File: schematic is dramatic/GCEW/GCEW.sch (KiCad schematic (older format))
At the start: 50 parts, among them J1 Conn_01x09_Male, J2 Conn_02x03_Odd_Even, J3 Conn_02x03_Odd_Even, J4 Conn_02x02_Odd_Even, M1 BLDC_Motor, U1 LM26CIM5-VHA, U2 DRV8323RH, U3 IPB029N06N, U4 IPB029N06N, U5 IPB029N06N, U6 IPB029N06N, U7 IPB029N06N, U8 IPB029N06N, U9 BLDC_Hall_Sensor

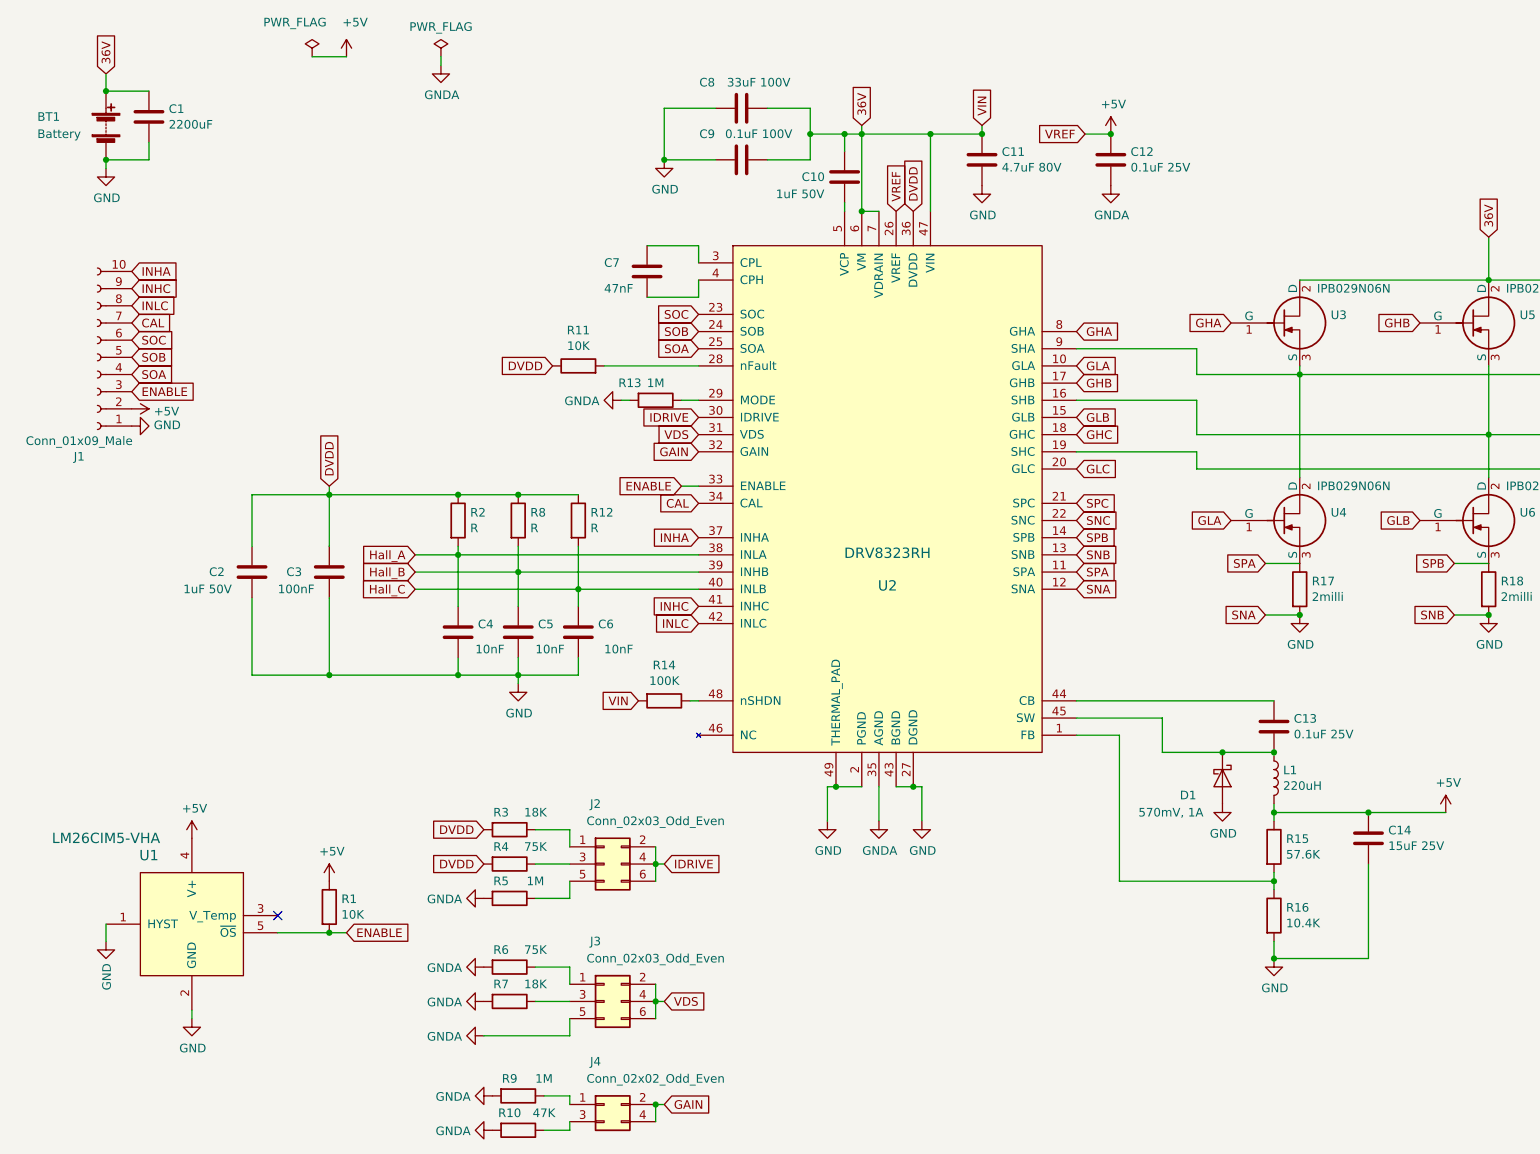
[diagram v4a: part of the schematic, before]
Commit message: GCEW Motor Controller Schematic Update 5
Finalized KiCAD GCEW Motor Controller Schematic. Initial KiCAD Motor Controller PCB Design.
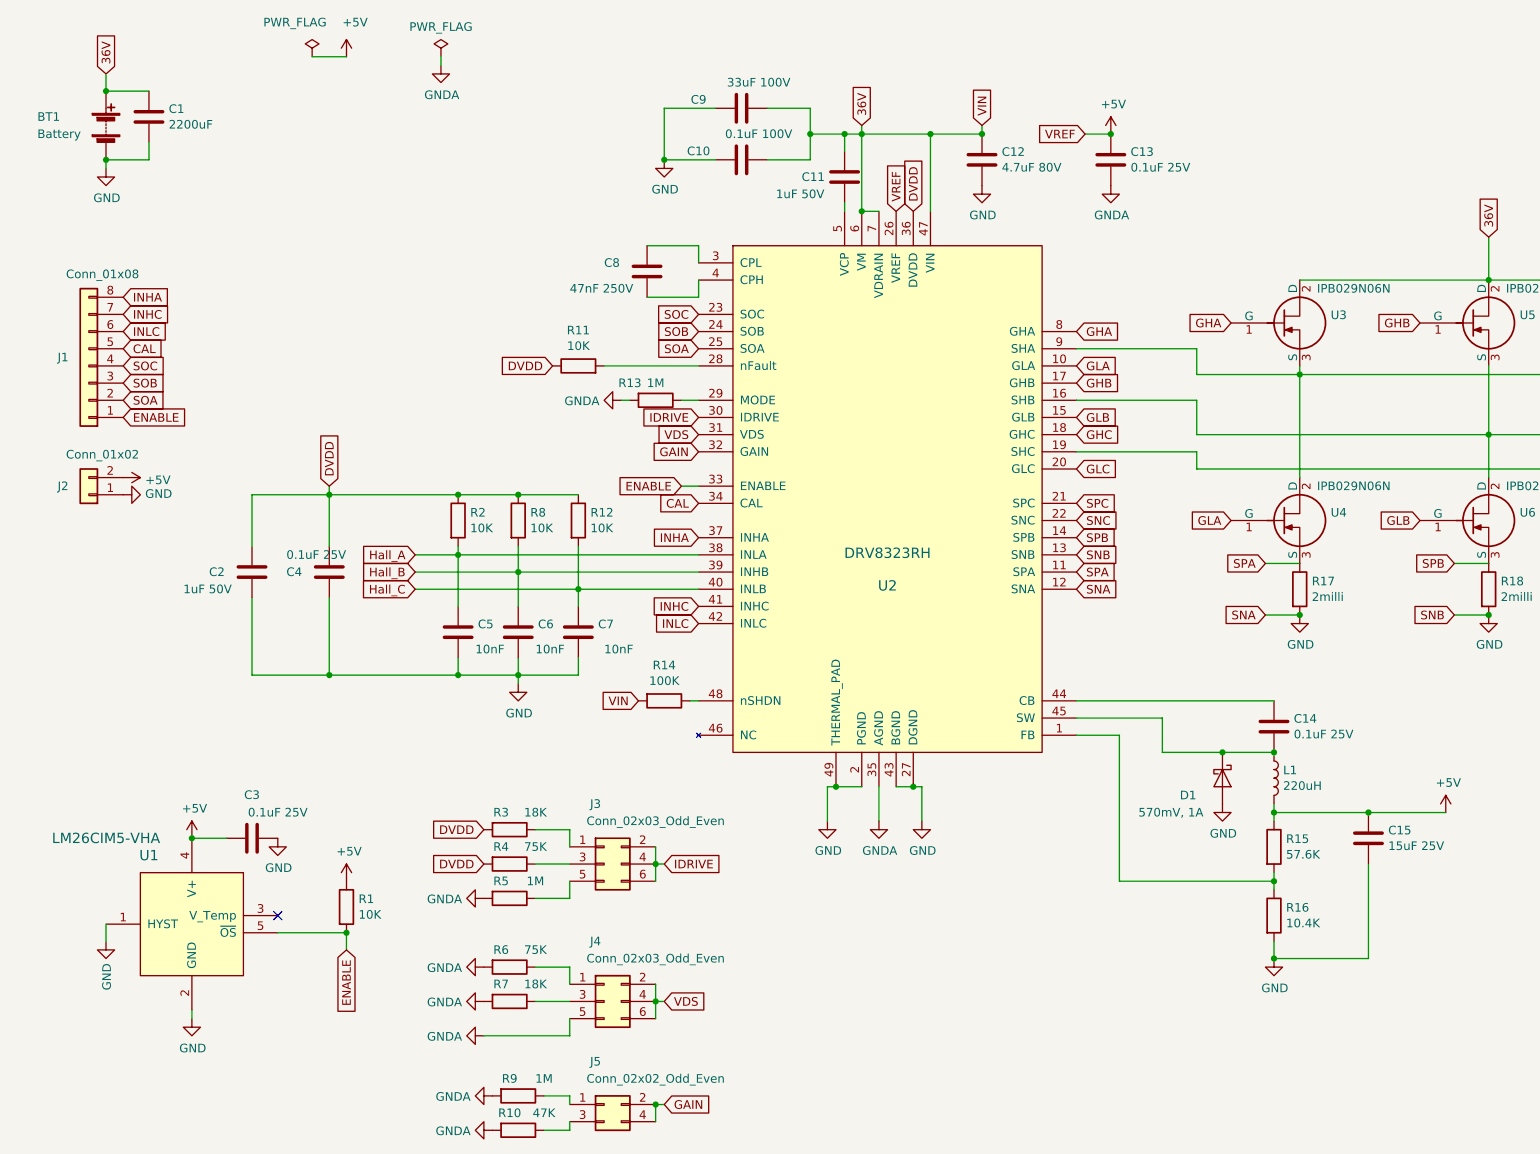
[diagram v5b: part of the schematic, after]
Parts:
- removed J1: Conn_01x09_Male, symbol Connector:Conn_01x10_Female
- added C3: 0.1uF 25V, Capacitors_SMD:C_1206, symbol Device:C
- added J1: Conn_01x08, myLib:PhoenixContact_1985027_8-Pin-Connector_8A_P3.5mm, symbol Connector_Generic:Conn_01x08
- added J2: Conn_01x02, myLib:PhoenixContact_1984963_2-Pin-Connector_8A_P3.5mm, symbol Connector_Generic:Conn_01x02
- BT1: footprint (none) -> myLib:PhoenixContact_1935776_2-Pin-Connector_32A_P5mm
- C1: footprint Capacitor_THT:CP_Radial_D18.0mm_P7.50mm -> Capacitors_THT:CP_Radial_D18.0mm_P7.50mm
- C10: renamed from C9; footprint Capacitor_SMD:C_1206_3216Metric -> Capacitors_SMD:C_1206
- C11: renamed from C10; footprint Capacitor_SMD:C_1206_3216Metric -> Capacitors_SMD:C_1206
- C12: renamed from C11; footprint CAPAE430X550N:CAPAE430X550N -> myLib:CP_Elec_6.6x6.6mm
- C13: renamed from C12; footprint Capacitor_SMD:C_1206_3216Metric -> Capacitors_SMD:C_1206
- C14: renamed from C13; footprint Capacitor_SMD:C_1206_3216Metric -> Capacitors_SMD:C_1206
- C15: renamed from C14; footprint 25TQC15MYFB:CAPPM3528X200N -> myLib:CP_Tantalum_Case-3528
- C2: footprint Capacitor_SMD:C_1206_3216Metric -> Capacitors_SMD:C_1206
- C4: renamed from C3; value 100nF -> 0.1uF 25V; footprint Capacitor_SMD:C_1206_3216Metric -> Capacitors_SMD:C_1206
- C5: renamed from C4; footprint Capacitor_SMD:C_1206_3216Metric -> Capacitors_SMD:C_0805
- C6: renamed from C5; footprint Capacitor_SMD:C_1206_3216Metric -> Capacitors_SMD:C_0805
- C7: renamed from C6; footprint Capacitor_SMD:C_1206_3216Metric -> Capacitors_SMD:C_0805
- C8: renamed from C7; value 47nF -> 47nF 250V; footprint Capacitor_SMD:C_1206_3216Metric -> Capacitors_SMD:C_1206
- C9: renamed from C8; footprint Capacitor_THT:CP_Radial_D10.0mm_P5.00mm -> Capacitors_THT:CP_Radial_D10.0mm_P5.00mm
- D1: footprint SOT1061:SOT1061 -> Diodes_SMD:D_SOD-123F
- J3: renamed from J2; footprint (none) -> Pin_Headers:Pin_Header_Straight_2x03_Pitch2.54mm
- J4: renamed from J3; footprint (none) -> Pin_Headers:Pin_Header_Straight_2x03_Pitch2.54mm
- J5: renamed from J4; footprint (none) -> Pin_Headers:Pin_Header_Straight_2x02_Pitch2.54mm
- L1: footprint CLF10060NIT-1R0N-D:INDPM101100X630N -> myLib:CLF10060NIT-221M-D
- M1: footprint (none) -> myLib:PhoenixContact_1991309_3-Pin-Connector_32A_P5mm
- R1, R10, R11, R13, R14, R3, R4, R5, R6, R7, R9: footprint Resistor_SMD:R_1206_3216Metric -> Resistors_SMD:R_1206
- R12, R2, R8: value R -> 10K; footprint Resistor_SMD:R_1206_3216Metric -> Resistors_SMD:R_1206
- R15, R16: footprint Resistor_SMD:R_0805_2012Metric -> Resistors_SMD:R_0805
- R17, R18, R19: footprint Resistor_SMD:R_1206_3216Metric -> Resistors_SMD:R_2512
- U1: footprint Package_TO_SOT_SMD:SOT-23-5 -> myLib:SOT-23-5
- U3, U4, U5, U6, U7, U8: footprint Package_TO_SOT_SMD:TO-263-2 -> myLib:TO-263-2
- U9: footprint (none) -> myLib:PhoenixContact_1984992_5-Pin-Connector_8A_P3.5mm
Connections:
- net +5V: now also C3.2, J2.2 (Pin_2)
- net CAL: now also J1.5 (Pin_5)
- net ENABLE: now also J1.1 (Pin_1)
- net GND: now also C3.1, J2.1 (Pin_1)
- net INHA: now also J1.8 (Pin_8)
- net INHC: now also J1.7 (Pin_7)
- net INLC: now also J1.6 (Pin_6)
- net SOA: now also J1.2 (Pin_2)
- net SOB: now also J1.3 (Pin_3)
- net SOC: now also J1.4 (Pin_4)
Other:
- moved on the sheet: R1

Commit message: GCEW Motor Controller Schematic Update 5
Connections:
- net GNDA is gone; now on net GND: C13.2, J4.5 (Pin_5), R10.2, R13.2, R5.2, R6.2, R7.2, R9.2, U2.35 (AGND)
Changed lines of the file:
@@
 	4450 1900 4150 1900
 $Comp
-L power:GNDA #PWR021
+L power:GNDA #PWR022
 U 1 1 5BDA2FAD
 P 5500 5250
-F 0 "#PWR021" H 5500 5000 50  0001 C CNN
+F 0 "#PWR022" H 5500 5000 50  0001 C CNN
 F 1 "GNDA" H 5505 5077 50  0000 C CNN
 F 2 "" H 5500 5250 50  0001 C CNN
@@
 	5500 5250 5500 5050
 $Comp
-L power:GND #PWR022
+L power:GND #PWR023
 U 1 1 5BDA32CC
 P 5750 5250
-F 0 "#PWR022" H 5750 5000 50  0001 C CNN
+F 0 "#PWR023" H 5750 5000 50  0001 C CNN
 F 1 "GND" H 5755 5077 50  0000 C CNN
 F 2 "" H 5750 5250 50  0001 C CNN
@@
 $EndComp
 $Comp
-L power:GND #PWR020
+L power:GND #PWR021
 U 1 1 5BDA3307
 P 5200 5250
-F 0 "#PWR020" H 5200 5000 50  0001 C CNN
+F 0 "#PWR021" H 5200 5000 50  0001 C CNN
 F 1 "GND" H 5205 5077 50  0000 C CNN
 F 2 "" H 5200 5250 50  0001 C CNN
@@
 $EndComp
 $Comp
-L power:+5V #PWR029
+L power:+5V #PWR030
 U 1 1 5BDA56B5
 P 8800 5200
-F 0 "#PWR029" H 8800 5050 50  0001 C CNN
+F 0 "#PWR030" H 8800 5050 50  0001 C CNN
 F 1 "+5V" H 8815 5373 50  0000 C CNN
 F 2 "" H 8800 5200 50  0001 C CNN
@@
 	6900 4750 6650 4750
 $Comp
-L power:GND #PWR027
+L power:GND #PWR028
 U 1 1 5BDA6FAD
 P 7800 6050
-F 0 "#PWR027" H 7800 5800 50  0001 C CNN
+F 0 "#PWR028" H 7800 5800 50  0001 C CNN
 F 1 "GND" H 7805 5877 50  0000 C CNN
 F 2 "" H 7800 6050 50  0001 C CNN
@@
 Hall_C
 $Comp
-L power:GND #PWR033
+L power:GND #PWR034
 U 1 1 5BDAD196
 P 12550 3200
-F 0 "#PWR033" H 12550 2950 50  0001 C CNN
+F 0 "#PWR034" H 12550 2950 50  0001 C CNN
 F 1 "GND" H 12555 3027 50  0000 C CNN
 F 2 "" H 12550 3200 50  0001 C CNN
@@
 $EndComp
 $Comp
-L power:+5V #PWR032
+L power:+5V #PWR033
 U 1 1 5BDAD1EB
 P 12550 2800
-F 0 "#PWR032" H 12550 2650 50  0001 C CNN
+F 0 "#PWR033" H 12550 2650 50  0001 C CNN
 F 1 "+5V" H 12565 2973 50  0000 C CNN
 F 2 "" H 12550 2800 50  0001 C CNN
@@
 Text GLabel 6650 3700 2    50   Input ~ 0
 SNB
-Text GLabel 6650 3900 2    50   Input ~ 0
-SNA
 $Comp
 L Device:R R17
@@
 $EndComp
 $Comp
-L power:GND #PWR028
+L power:GND #PWR029
 U 1 1 5BDC102D
 P 7950 4050
-F 0 "#PWR028" H 7950 3800 50  0001 C CNN
+F 0 "#PWR029" H 7950 3800 50  0001 C CNN
 F 1 "GND" H 7955 3877 50  0000 C CNN
 F 2 "" H 7950 4050 50  0001 C CNN
@@
 	7950 4050 7750 4050
 Connection ~ 7950 4050
-Text GLabel 7750 4050 0    50   Input ~ 0
-SNA
 $Comp
 L Device:R R18
@@
 $EndComp
 $Comp
-L power:GND #PWR030
+L power:GND #PWR031
 U 1 1 5BDC23F0
 P 9050 4050
-F 0 "#PWR030" H 9050 3800 50  0001 C CNN
+F 0 "#PWR031" H 9050 3800 50  0001 C CNN
 F 1 "GND" H 9055 3877 50  0000 C CNN
 F 2 "" H 9050 4050 50  0001 C CNN
@@
 $EndComp
 $Comp
-L power:GND #PWR031
+L power:GND #PWR032
 U 1 1 5BDC242B
 P 10150 4050
-F 0 "#PWR031" H 10150 3800 50  0001 C CNN
+F 0 "#PWR032" H 10150 3800 50  0001 C CNN
 F 1 "GND" H 10155 3877 50  0000 C CNN
 F 2 "" H 10150 4050 50  0001 C CNN
@@
 	3750 3900 3750 3650
 $Comp
-L power:GND #PWR017
+L power:GND #PWR018
 U 1 1 5BE040E2
 P 3400 4450
-F 0 "#PWR017" H 3400 4200 50  0001 C CNN
+F 0 "#PWR018" H 3400 4200 50  0001 C CNN
 F 1 "GND" H 3405 4277 50  0000 C CNN
 F 2 "" H 3400 4450 50  0001 C CNN
@@
 Wire Wire Line
 	2400 800  2200 800
-$Comp
-L power:PWR_FLAG #FLG02
-U 1 1 5BE266D4
-P 2950 800
-F 0 "#FLG02" H 2950 875 50  0001 C CNN
-F 1 "PWR_FLAG" H 2950 974 50  0000 C CNN
-F 2 "" H 2950 800 50  0001 C CNN
-F 3 "~" H 2950 800 50  0001 C CNN
-	1    2950 800
-	1    0    0    -1
-$EndComp
-$Comp
-L power:GNDA #PWR010
-U 1 1 5BE2678E
-P 2950 850
-F 0 "#PWR010" H 2950 600 50  0001 C CNN
-F 1 "GNDA" H 2955 677 50  0000 C CNN
-F 2 "" H 2950 850 50  0001 C CNN
-F 3 "" H 2950 850 50  0001 C CNN
-	1    2950 850
-	1    0    0    -1
-$EndComp
-Wire Wire Line
-	2950 850  2950 800
 Text GLabel 2800 3700 0    50   Input ~ 0
 Hall_A
@@
 $EndComp
 $Comp
-L power:GND #PWR023
+L power:GND #PWR024
 U 1 1 5BD121CF
 P 6100 1550
-F 0 "#PWR023" H 6100 1300 50  0001 C CNN
+F 0 "#PWR024" H 6100 1300 50  0001 C CNN
 F 1 "GND" H 6105 1377 50  0000 C CNN
 F 2 "" H 6100 1550 50  0001 C CNN
@@
 	4350 2800 4450 2800
 $Comp
-L power:GNDA #PWR018
+L power:GNDA #PWR019
 U 1 1 5BD271E0
 P 4000 2800
-F 0 "#PWR018" H 4000 2550 50  0001 C CNN
+F 0 "#PWR019" H 4000 2550 50  0001 C CNN
 F 1 "GNDA" V 4005 2673 50  0000 R CNN
 F 2 "" H 4000 2800 50  0001 C CNN
@@
 	3700 7050 3700 7000
 $Comp
-L power:GNDA #PWR016
+L power:GNDA #PWR017
 U 1 1 5BD62495
 P 3250 7050
-F 0 "#PWR016" H 3250 6800 50  0001 C CNN
+F 0 "#PWR017" H 3250 6800 50  0001 C CNN
 F 1 "GNDA" V 3255 6923 50  0000 R CNN
 F 2 "" H 3250 7050 50  0001 C CNN
@@
 $EndComp
 $Comp
-L power:GNDA #PWR015
+L power:GNDA #PWR016
 U 1 1 5BD62647
 P 3250 6850
-F 0 "#PWR015" H 3250 6600 50  0001 C CNN
+F 0 "#PWR016" H 3250 6600 50  0001 C CNN
 F 1 "GNDA" V 3255 6723 50  0000 R CNN
 F 2 "" H 3250 6850 50  0001 C CNN
@@
 DVDD
 $Comp
-L power:GNDA #PWR011
+L power:GNDA #PWR012
 U 1 1 5BD6A69F
 P 3200 5700
-F 0 "#PWR011" H 3200 5450 50  0001 C CNN
+F 0 "#PWR012" H 3200 5450 50  0001 C CNN
 F 1 "GNDA" V 3205 5573 50  0000 R CNN
 F 2 "" H 3200 5700 50  0001 C CNN
@@
 	3700 5700 3700 5600
 $Comp
-L power:GNDA #PWR014
+L power:GNDA #PWR015
 U 1 1 5BD6EFD8
 P 3200 6500
-F 0 "#PWR014" H 3200 6250 50  0001 C CNN
+F 0 "#PWR015" H 3200 6250 50  0001 C CNN
 F 1 "GNDA" V 3205 6373 50  0000 R CNN
 F 2 "" H 3200 6500 50  0001 C CNN
@@
 	3200 6500 3700 6500
 $Comp
-L power:GNDA #PWR013
+L power:GNDA #PWR014
 U 1 1 5BD73A82
 P 3200 6300
-F 0 "#PWR013" H 3200 6050 50  0001 C CNN
+F 0 "#PWR014" H 3200 6050 50  0001 C CNN
 F 1 "GNDA" V 3205 6173 50  0000 R CNN
 F 2 "" H 3200 6300 50  0001 C CNN
@@
 $EndComp
 $Comp
-L power:GNDA #PWR012
+L power:GNDA #PWR013
 U 1 1 5BD73AE7
 P 3200 6100
-F 0 "#PWR012" H 3200 5850 50  0001 C CNN
+F 0 "#PWR013" H 3200 5850 50  0001 C CNN
 F 1 "GNDA" V 3205 5973 50  0000 R CNN
 F 2 "" H 3200 6100 50  0001 C CNN
@@
 $EndComp
 $Comp
-L power:GNDA #PWR025
+L power:GNDA #PWR026
 U 1 1 5BDD38EC
 P 6850 1550
-F 0 "#PWR025" H 6850 1300 50  0001 C CNN
+F 0 "#PWR026" H 6850 1300 50  0001 C CNN
 F 1 "GNDA" H 6855 1377 50  0000 C CNN
 F 2 "" H 6850 1550 50  0001 C CNN
@@
 $EndComp
 $Comp
-L power:+5V #PWR024
+L power:+5V #PWR025
 U 1 1 5BDD44D6
 P 6850 1250
-F 0 "#PWR024" H 6850 1100 50  0001 C CNN
+F 0 "#PWR025" H 6850 1100 50  0001 C CNN
 F 1 "+5V" H 6865 1423 50  0000 C CNN
 F 2 "" H 6850 1250 50  0001 C CNN
@@
 Connection ~ 7500 4850
 $Comp
-L power:GND #PWR026
+L power:GND #PWR027
 U 1 1 5BE016E5
 P 7500 5150
-F 0 "#PWR026" H 7500 4900 50  0001 C CNN
+F 0 "#PWR027" H 7500 4900 50  0001 C CNN
 F 1 "GND" H 7505 4977 50  0000 C CNN
 F 2 "" H 7500 5150 50  0001 C CNN
@@
 $EndComp
 $Comp
-L power:GND #PWR019
+L power:GND #PWR020
 U 1 1 5BE19469
 P 4250 1400
-F 0 "#PWR019" H 4250 1150 50  0001 C CNN
+F 0 "#PWR020" H 4250 1150 50  0001 C CNN
 F 1 "GND" H 4255 1227 50  0000 C CNN
 F 2 "" H 4250 1400 50  0001 C CNN
@@
 	2400 6000 2400 5900
 Connection ~ 2400 5900
+$Comp
+L power:GND #PWR010
+U 1 1 5BD446A0
+P 2750 650
+F 0 "#PWR010" H 2750 400 50  0001 C CNN
+F 1 "GND" H 2755 477 50  0000 C CNN
+F 2 "" H 2750 650 50  0001 C CNN
+F 3 "" H 2750 650 50  0001 C CNN
+	1    2750 650
+	1    0    0    -1
+$EndComp
+$Comp
+L power:GNDA #PWR011
+U 1 1 5BD44746
+P 2950 650
+F 0 "#PWR011" H 2950 400 50  0001 C CNN
+F 1 "GNDA" H 2955 477 50  0000 C CNN
+F 2 "" H 2950 650 50  0001 C CNN
+F 3 "" H 2950 650 50  0001 C CNN
+	1    2950 650
+	1    0    0    -1
+$EndComp
+Wire Wire Line
+	2750 650  2950 650
+Text GLabel 7750 4050 0    50   Input ~ 0
+SNA
+Text GLabel 6650 3900 2    50   Input ~ 0
+SNA
 $EndSCHEMATC

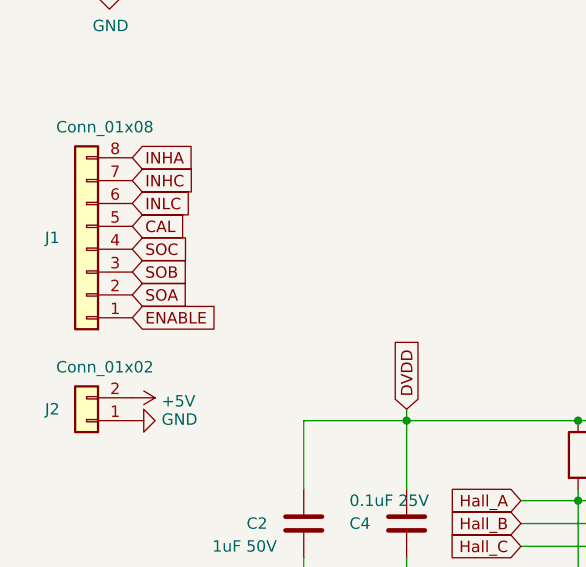
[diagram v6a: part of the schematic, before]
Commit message: GCEW Motor Controller PCB Update 1
17 Connections left to complete. Still need to finalize board outline dimensions.
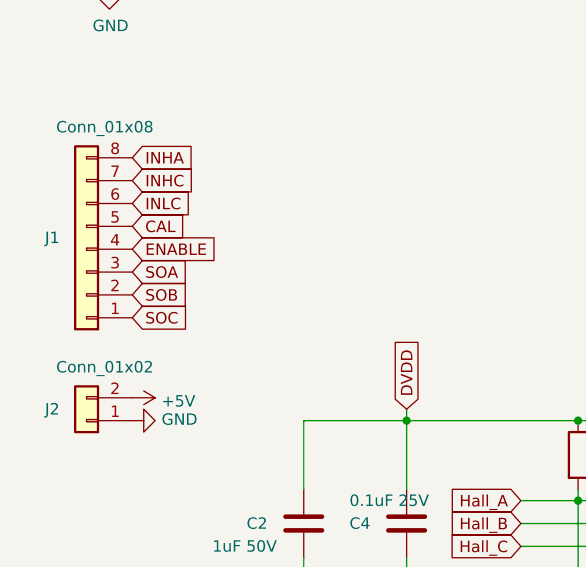
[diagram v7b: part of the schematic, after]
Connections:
- net ENABLE: now also J1.4 (Pin_4); no longer J1.1 (Pin_1)
- net SOA: now also J1.3 (Pin_3); no longer J1.2 (Pin_2)
- net SOB: now also J1.2 (Pin_2); no longer J1.3 (Pin_3)
- net SOC: now also J1.1 (Pin_1); no longer J1.4 (Pin_4)
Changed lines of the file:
@@
 Text GLabel 1100 2500 2    50   Input ~ 0
 CAL
+Text GLabel 1100 2700 2    50   Input ~ 0
+SOA
 Text GLabel 1100 2800 2    50   Input ~ 0
-SOA
-Text GLabel 1100 2700 2    50   Input ~ 0
 SOB
-Text GLabel 1100 2600 2    50   Input ~ 0
+Text GLabel 1100 2900 2    50   Input ~ 0
 SOC
 $Comp
@@
 	4200 6900 4250 6900
 Connection ~ 4200 6900
-Text GLabel 1100 2900 2    50   Input ~ 0
+Text GLabel 1100 2600 2    50   Input ~ 0
 ENABLE
 Wire Wire Line

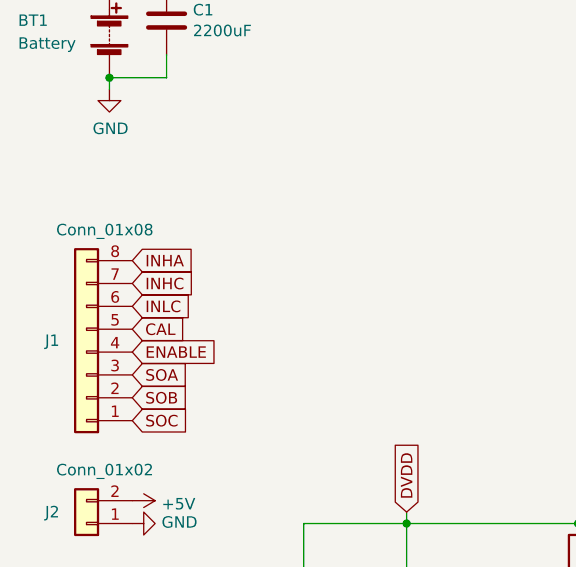
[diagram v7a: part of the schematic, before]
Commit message: GCEW Motor Controller PCB Update 1
Completed GCEW Motor Controller PCB Design.
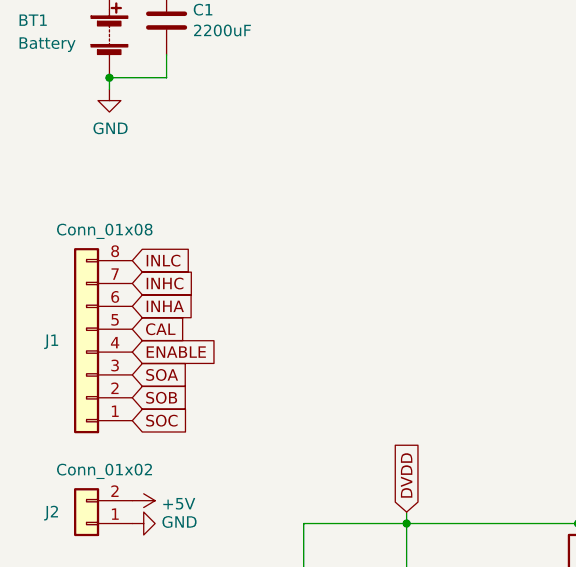
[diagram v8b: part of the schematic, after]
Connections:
- net INHA: now also J1.6 (Pin_6); no longer J1.8 (Pin_8)
- net INLC: now also J1.8 (Pin_8); no longer J1.6 (Pin_6)
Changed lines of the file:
@@
 Text GLabel 2400 6000 3    50   Input ~ 0
 ENABLE
-Text GLabel 1100 2200 2    50   Input ~ 0
+Text GLabel 1100 2400 2    50   Input ~ 0
 INHA
 Text GLabel 1100 2300 2    50   Input ~ 0
 INHC
-Text GLabel 1100 2400 2    50   Input ~ 0
+Text GLabel 1100 2200 2    50   Input ~ 0
 INLC
 Text GLabel 1100 2500 2    50   Input ~ 0
